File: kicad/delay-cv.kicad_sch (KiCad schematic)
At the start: 29 parts, among them Q4 2N3904, Q5 2N3904, U7 TL074

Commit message: Removing test points from BOM
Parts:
- TP12, TP8: now left out of the parts list
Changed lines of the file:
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@@
   )
   (symbol (lib_id "Connector:TestPoint") (at 196.85 72.39 0) (unit 1)
-    (in_bom yes) (on_board yes) (dnp no) (fields_autoplaced)
+    (in_bom no) (on_board yes) (dnp no) (fields_autoplaced)
     (property "Reference" "TP12" (at 198.247 68.2533 0)
       (effects (font (size 1.27 1.27)) (justify left))
@@
   )
   (symbol (lib_id "Connector:TestPoint") (at 152.4 63.5 0) (unit 1)
-    (in_bom yes) (on_board yes) (dnp no) (fields_autoplaced)
+    (in_bom no) (on_board yes) (dnp no) (fields_autoplaced)
     (property "Reference" "TP8" (at 153.797 59.3633 0)
       (effects (font (size 1.27 1.27)) (justify left))

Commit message: Changing decoupling caps to ceramic X7R
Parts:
- C35, C37: Spec ceramic C0G -> ceramic X7R
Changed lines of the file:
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@@
       (effects (font (size 1.27 1.27)) hide)
     )
-    (property "Spec" "ceramic C0G" (at 140.97 153.67 90)
+    (property "Spec" "ceramic X7R" (at 140.97 153.67 90)
       (effects (font (size 1.27 1.27)) hide)
     )
@@
       (effects (font (size 1.27 1.27)) hide)
     )
-    (property "Spec" "ceramic C0G" (at 140.97 166.37 90)
-      (effects (font (size 1.27 1.27)) hide)
-    )
+    (property "Spec" "ceramic X7R" (at 140.97 166.37 90)
+      (effects (font (size 1.27 1.27)) hide)
+    )

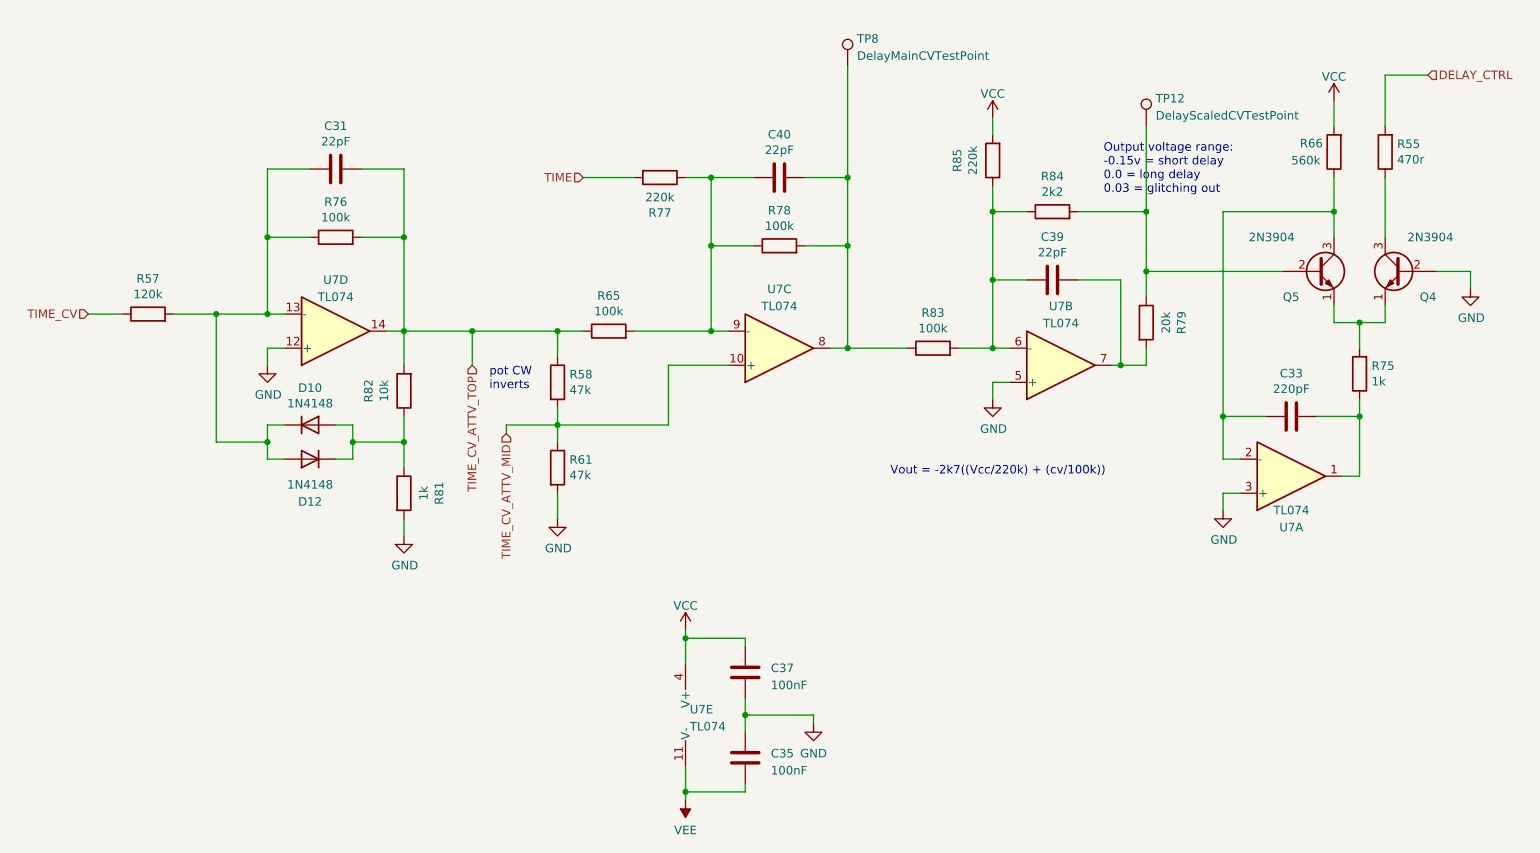
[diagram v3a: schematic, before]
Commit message: Updating board for new footprint libraries
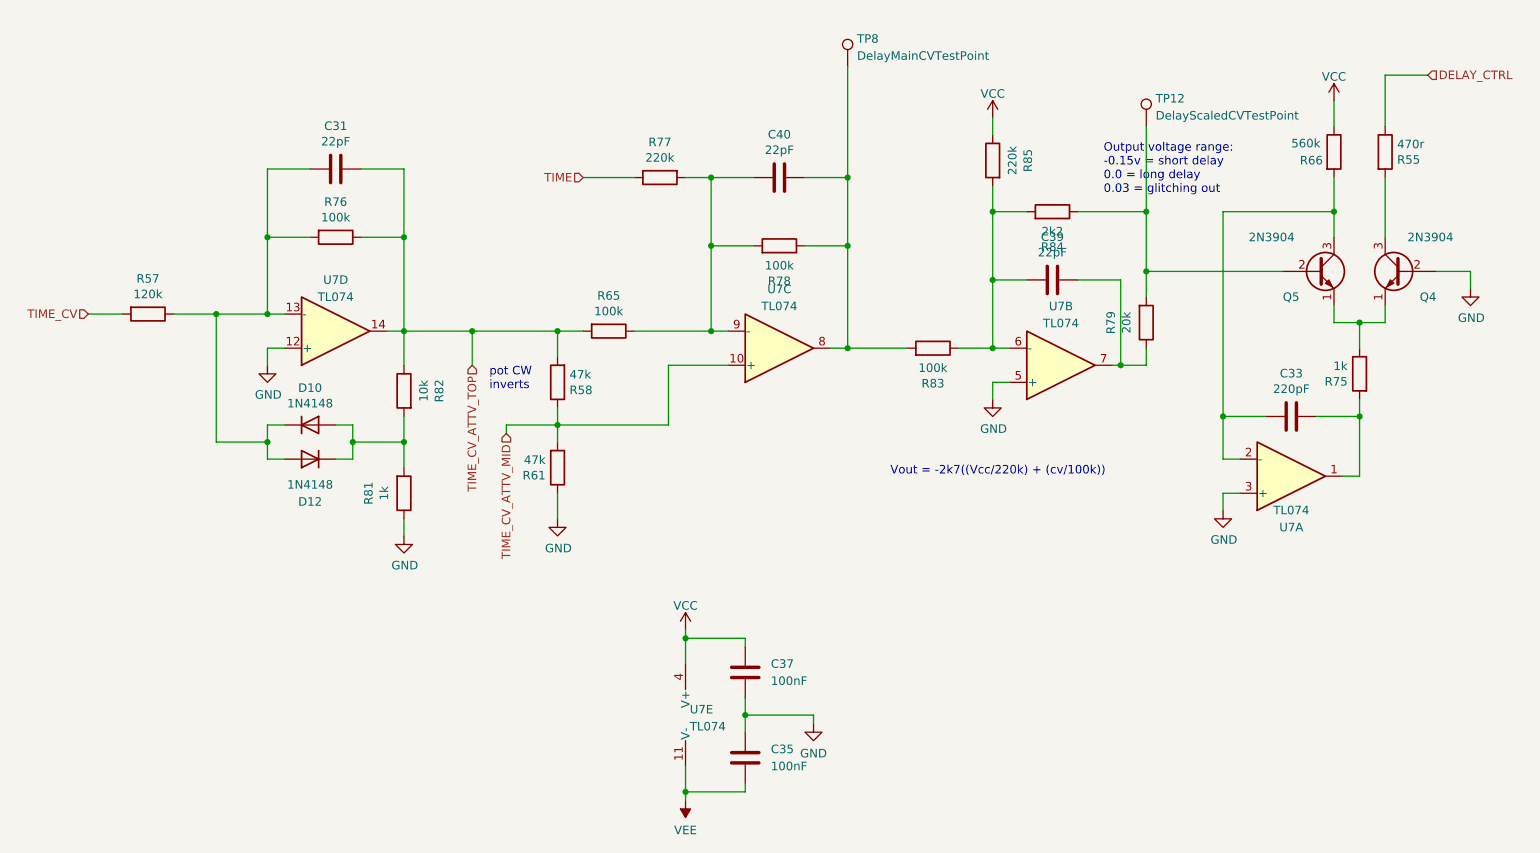
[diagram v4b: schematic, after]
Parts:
- C31, C33, C35, C37, C39, C40: symbol Rumblesan Standard Parts:C -> Rumblesan_Standard_Parts:C
- Q4, Q5: footprint Rumblesan_Standard_Parts:TO-92_Inline_Wide -> Package_TO_SOT_THT:TO-92_Inline_Wide
- R55, R57, R58, R61, R65, R66, R75, R76, R77, R78, R79, R81, R82, R83, R84, R85: symbol Rumblesan Standard Parts:R -> Rumblesan_Standard_Parts:R
- U7: footprint Rumblesan_Standard_Parts:DIP-14_W7.62mm_Socket -> Package_DIP:DIP-14_W7.62mm_Socket
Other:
- moved on the sheet: R57, R58, R61, R65, R75, R76, R77, R78, R79, R81, R82, R83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

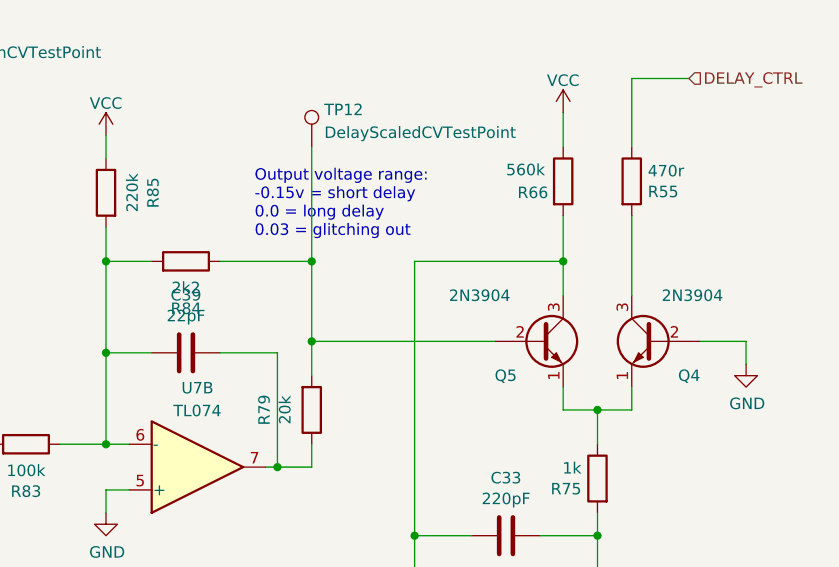
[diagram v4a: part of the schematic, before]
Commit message: Updating with rev03 changes
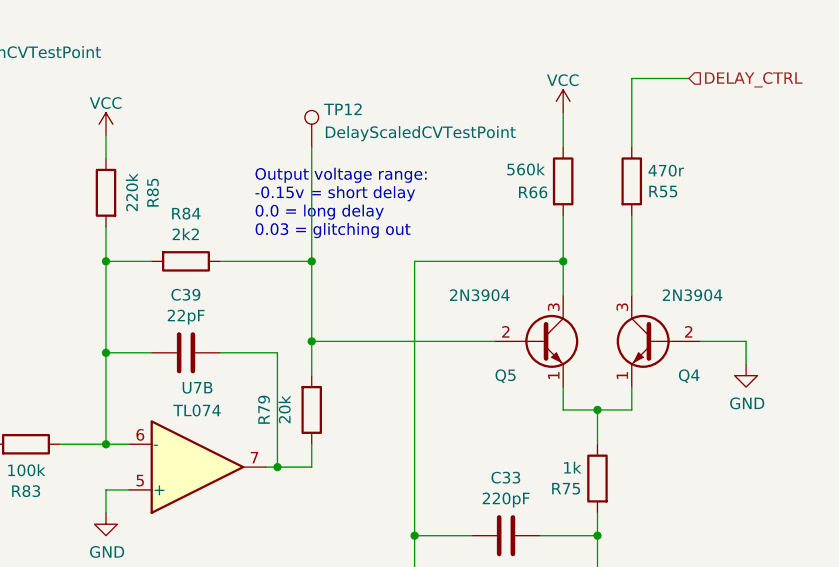
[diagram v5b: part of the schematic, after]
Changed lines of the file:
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@@
 (kicad_sch
-	(version 20231120)
+	(version 20250114)
 	(generator "eeschema")
-	(generator_version "8.0")
+	(generator_version "9.0")
 	(paper "A4")
 	(title_block
@@
 		(comment 4 "Author: Guy John")
 	)
+	(text "Vout = -2k7((Vcc/220k) + (cv/100k))"
+		(exclude_from_sim no)
+		(at 158.75 124.46 0)
+		(effects
+			(font
+				(size 1.27 1.27)
+			)
+			(justify left bottom)
+		)
+	)
+	(text "Output voltage range:\n-0.15v = short delay\n0.0 = long delay\n0.03 = glitching out"
+		(exclude_from_sim no)
+		(at 190.5 82.55 0)
+		(effects
+			(font
+				(size 1.27 1.27)
+			)
+			(justify left bottom)
+		)
+	)
+	(text "pot CW\ninverts"
+		(exclude_from_sim no)
+		(at 99.06 111.76 0)
+		(effects
+			(font
+				(size 1.27 1.27)
+			)
+			(justify left bottom)
+		)
+	)
 	(junction
 		(at 137.16 160.02)
@@
 		)
 	)
-	(text "Vout = -2k7((Vcc/220k) + (cv/100k))"
-		(exclude_from_sim no)
-		(at 158.75 124.46 0)
-		(effects
-			(font
-				(size 1.27 1.27)
-			)
-			(justify left bottom)
-		)
-	)
-	(text "Output voltage range:\n-0.15v = short delay\n0.0 = long delay\n0.03 = glitching out"
-		(exclude_from_sim no)
-		(at 190.5 82.55 0)
-		(effects
-			(font
-				(size 1.27 1.27)
-			)
-			(justify left bottom)
-		)
-	)
-	(text "pot CW\ninverts"
-		(exclude_from_sim no)
-		(at 99.06 111.76 0)
-		(effects
-			(font
-				(size 1.27 1.27)
-			)
-			(justify left bottom)
-		)
-	)
 	(hierarchical_label "TIME_CV_ATTV_TOP"
 		(shape input)
 		(at 96.52 107.95 270)
-		(fields_autoplaced yes)
 		(effects
 			(font
@@
 		(shape input)
 		(at 238.76 64.77 0)
-		(fields_autoplaced yes)
 		(effects
 			(font
@@
 		(shape input)
 		(at 101.6 118.11 270)
-		(fields_autoplaced yes)
 		(effects
 			(font
@@
 		(shape input)
 		(at 113.03 80.01 180)
-		(fields_autoplaced yes)
 		(effects
 			(font
@@
 		(shape input)
 		(at 39.37 100.33 180)
-		(fields_autoplaced yes)
 		(effects
 			(font
@@
 		(lib_id "Rumblesan_Standard_Parts:R")
 		(at 182.88 85.09 90)
+		(mirror x)
 		(unit 1)
 		(exclude_from_sim no)
@@
 		(dnp no)
 		(property "Reference" "R84"
-			(at 182.88 90.3478 90)
+			(at 182.88 79.8322 90)
 			(effects
 				(font
@@
 		)
 		(property "Value" "2k2"
-			(at 182.88 88.0364 90)
+			(at 182.88 82.1436 90)
 			(effects
 				(font
@@
 		)
 		(property "Footprint" "Rumblesan_Standard_Parts:R_Axial_DIN0207_L6.3mm_D2.5mm_P10.16mm_Horizontal"
-			(at 185.42 82.55 90)
+			(at 185.42 87.63 90)
 			(effects
 				(font
@@
 		)
 		(property "Datasheet" "~"
-			(at 182.88 78.74 90)
+			(at 182.88 91.44 90)
 			(effects
 				(font
@@
 		)
 		(property "Spec" "metal film"
-			(at 182.88 80.01 90)
+			(at 182.88 90.17 90)
 			(effects
 				(font
@@
 		)
 		(property "Tolerance" "1%"
-			(at 189.23 80.01 90)
+			(at 189.23 90.17 90)
 			(effects
 				(font
@@
 		)
 		(property "Power" "0.5W"
-			(at 175.26 80.01 90)
+			(at 175.26 90.17 90)
 			(effects
 				(font
@@
 			)
 		)
-		(property "Description" ""
+		(property "Description" "0.2A Ic, 40V Vce, Small Signal NPN Transistor, TO-92"
 			(at 222.25 93.98 0)
 			(effects
@@
 			)
 		)
-		(property "Description" ""
+		(property "Description" "0.2A Ic, 40V Vce, Small Signal NPN Transistor, TO-92"
 			(at 234.95 93.98 0)
 			(effects

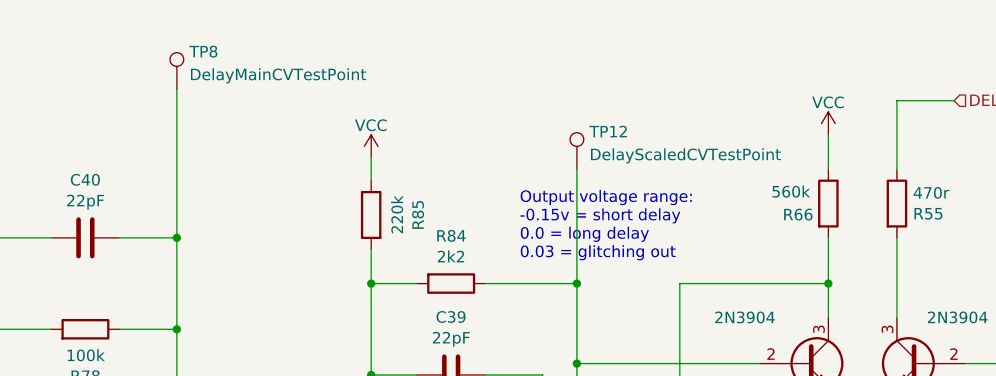
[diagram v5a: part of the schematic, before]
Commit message: Digital ground for divider and other layout improvements
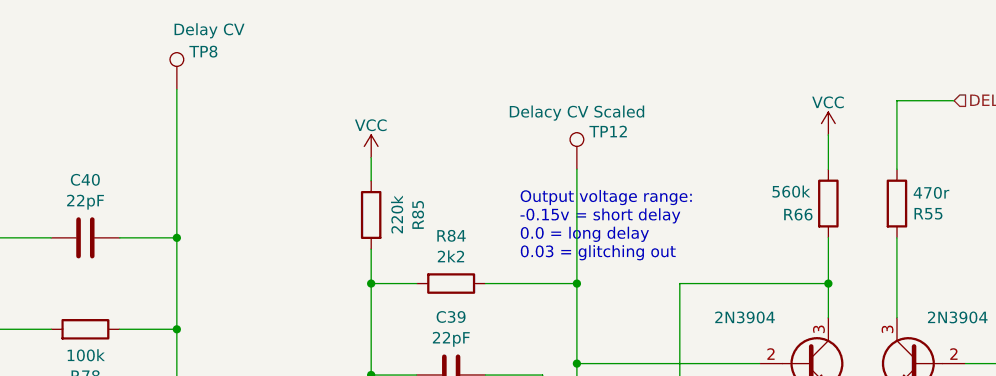
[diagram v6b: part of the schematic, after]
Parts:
- TP12: value DelayScaledCVTestPoint -> TestPoint; Name (none) -> Delacy CV Scaled
- TP8: value DelayMainCVTestPoint -> TestPoint; Name (none) -> Delay CV
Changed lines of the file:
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@@
 		(on_board yes)
 		(dnp no)
-		(fields_autoplaced yes)
 		(property "Reference" "TP12"
 			(at 198.247 68.2533 0)
@@
 			)
 		)
-		(property "Value" "DelayScaledCVTestPoint"
+		(property "Value" "TestPoint"
 			(at 198.247 70.7902 0)
 			(effects
@@
 				)
 				(justify left)
+				(hide yes)
 			)
 		)
@@
 				)
 				(hide yes)
+			)
+		)
+		(property "Name" "Delacy CV Scaled"
+			(at 196.85 66.04 0)
+			(effects
+				(font
+					(size 1.27 1.27)
+				)
 			)
 		)
@@
 		(on_board yes)
 		(dnp no)
-		(fields_autoplaced yes)
 		(property "Reference" "TP8"
 			(at 153.797 59.3633 0)
@@
 			)
 		)
-		(property "Value" "DelayMainCVTestPoint"
+		(property "Value" "TestPoint"
 			(at 153.797 61.9002 0)
 			(effects
@@
 				)
 				(justify left)
+				(hide yes)
 			)
 		)
@@
 			)
 		)
+		(property "Name" "Delay CV"
+			(at 155.956 56.896 0)
+			(effects
+				(font
+					(size 1.27 1.27)
+				)
+			)
+		)
